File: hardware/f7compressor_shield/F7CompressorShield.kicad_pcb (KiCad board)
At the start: 2 copper layers, 148 x 168 mm, 12 parts, among them CN10 PinSocket_2x17_P2.54mm_Vertic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, CN7 PinSocket_2x10_P2.54mm_Vertic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, CN8 PinSocket_2x08_P2.54mm_Vertic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, CN9 PinSocket_2x15_P2.54mm_Vertic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, J1 PinSocket_2x17_P2.54mm_Vertic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, J2 PinHeader_1x06_P2.54mm_Vertic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, J3 TerminalBlock_MaiXu_MX126-5.0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, J4 TerminalBlock_MaiXu_MX126-5.0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, J5 TerminalBlock_MaiXu_MX126-5.0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, U1 ST_Morpho_Connector_144_STLink

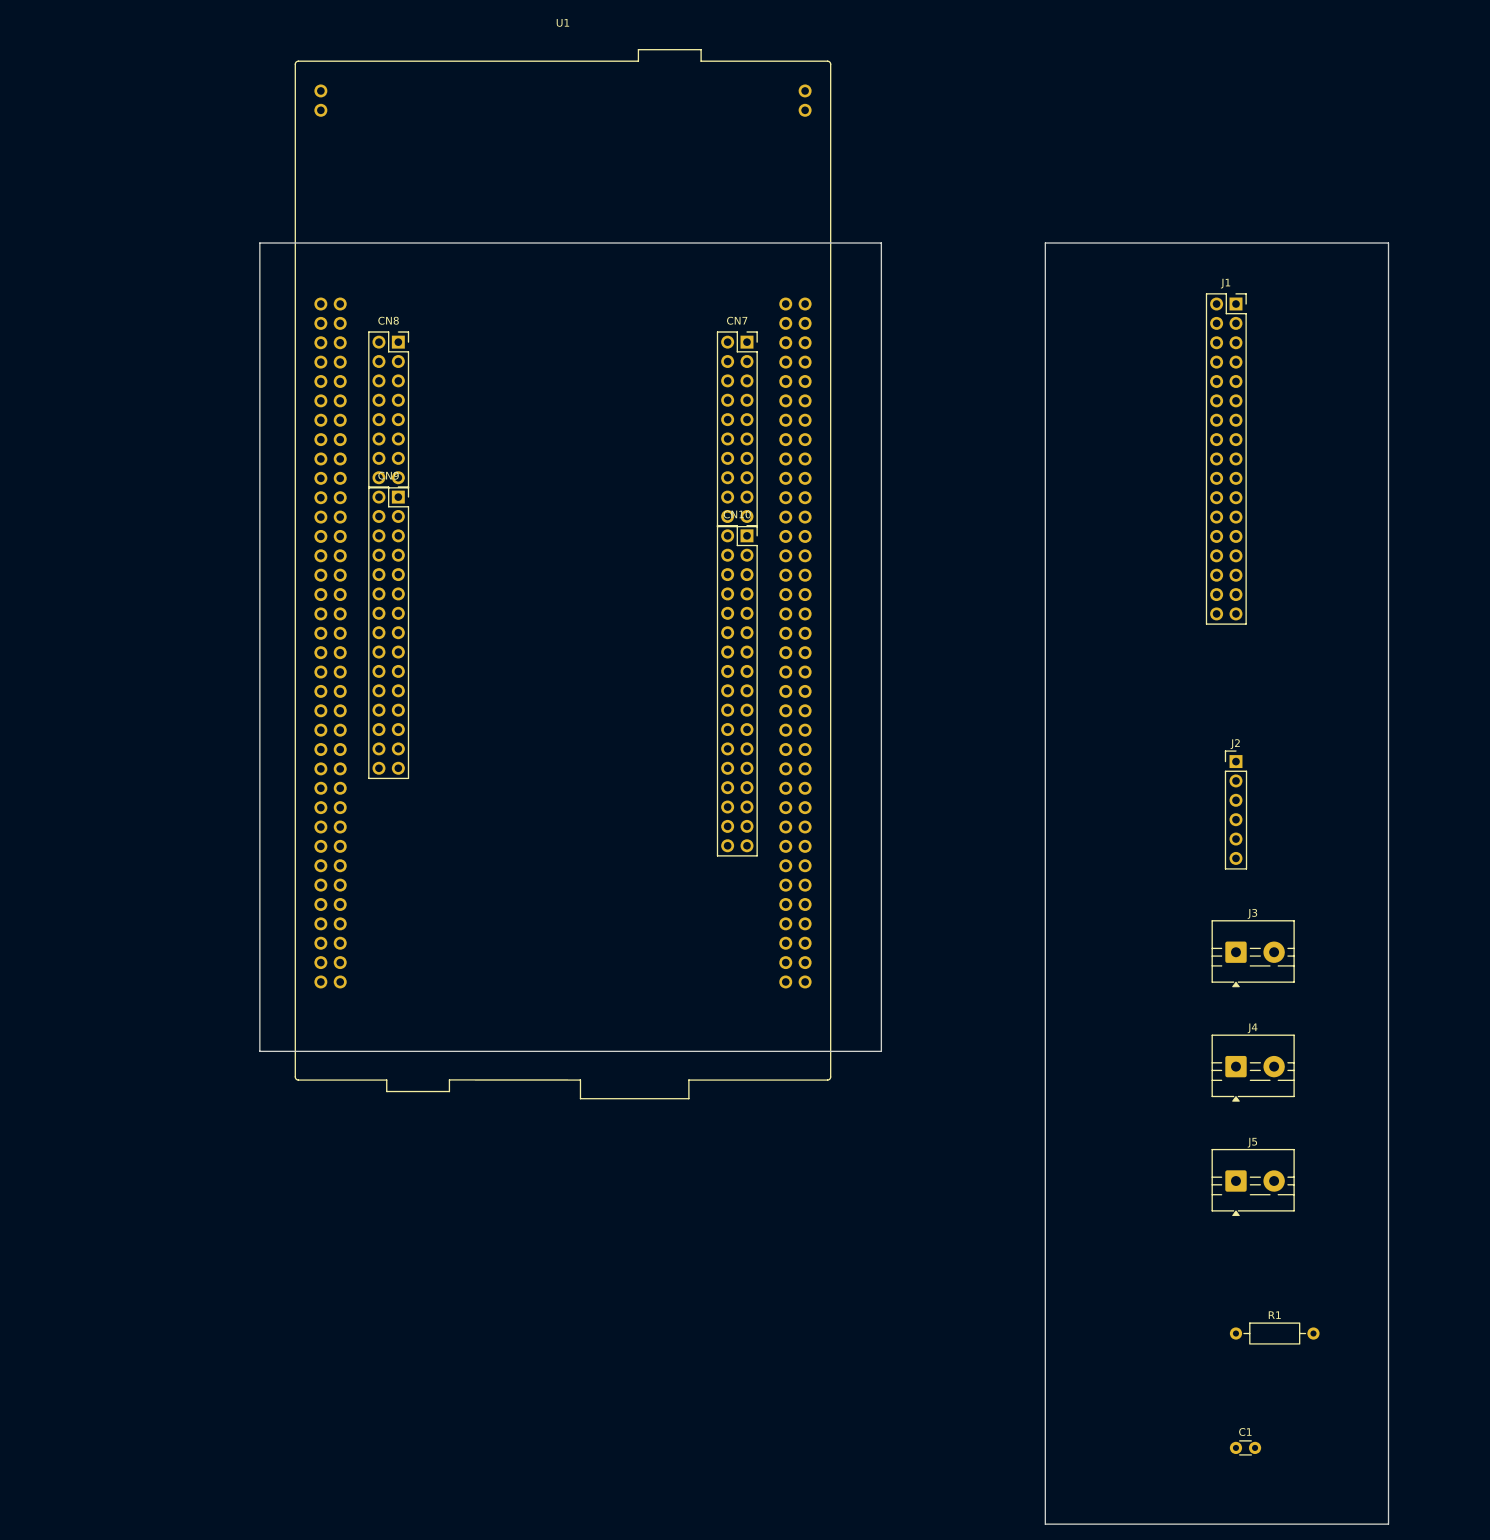
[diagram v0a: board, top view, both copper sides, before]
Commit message: Fix Zio/LCD header pin-1 orientation on shield PCB; re-route
Pin 1's physical column (and its square silkscreen marker) didn't match
the real Nucleo/LCD silkscreen on CN7-CN10 and J1 -- the generic KiCad
Odd_Even footprint's pad 1/2 assignment is mirrored relative to the real
boards. Fixed by mirroring the footprints themselves (not swapping net
assignments, which is electrically equivalent but leaves the pin-1
marker in the wrong physical spot). Also fixed 3 clearance violations
left by the re-route and confirmed CN12/FMC pin alternate-function
questions against the Nucleo schematic and MCU datasheet -- no other
conflicts beyond the already-documented PD8/PD9 VCP/FMC_D13-D14 reuse.

ERC clean, DRC 0 unconnected items, same expected-findings baseline.

Co-Authored-By: Claude Sonnet 5 <noreply@anthropic.com>
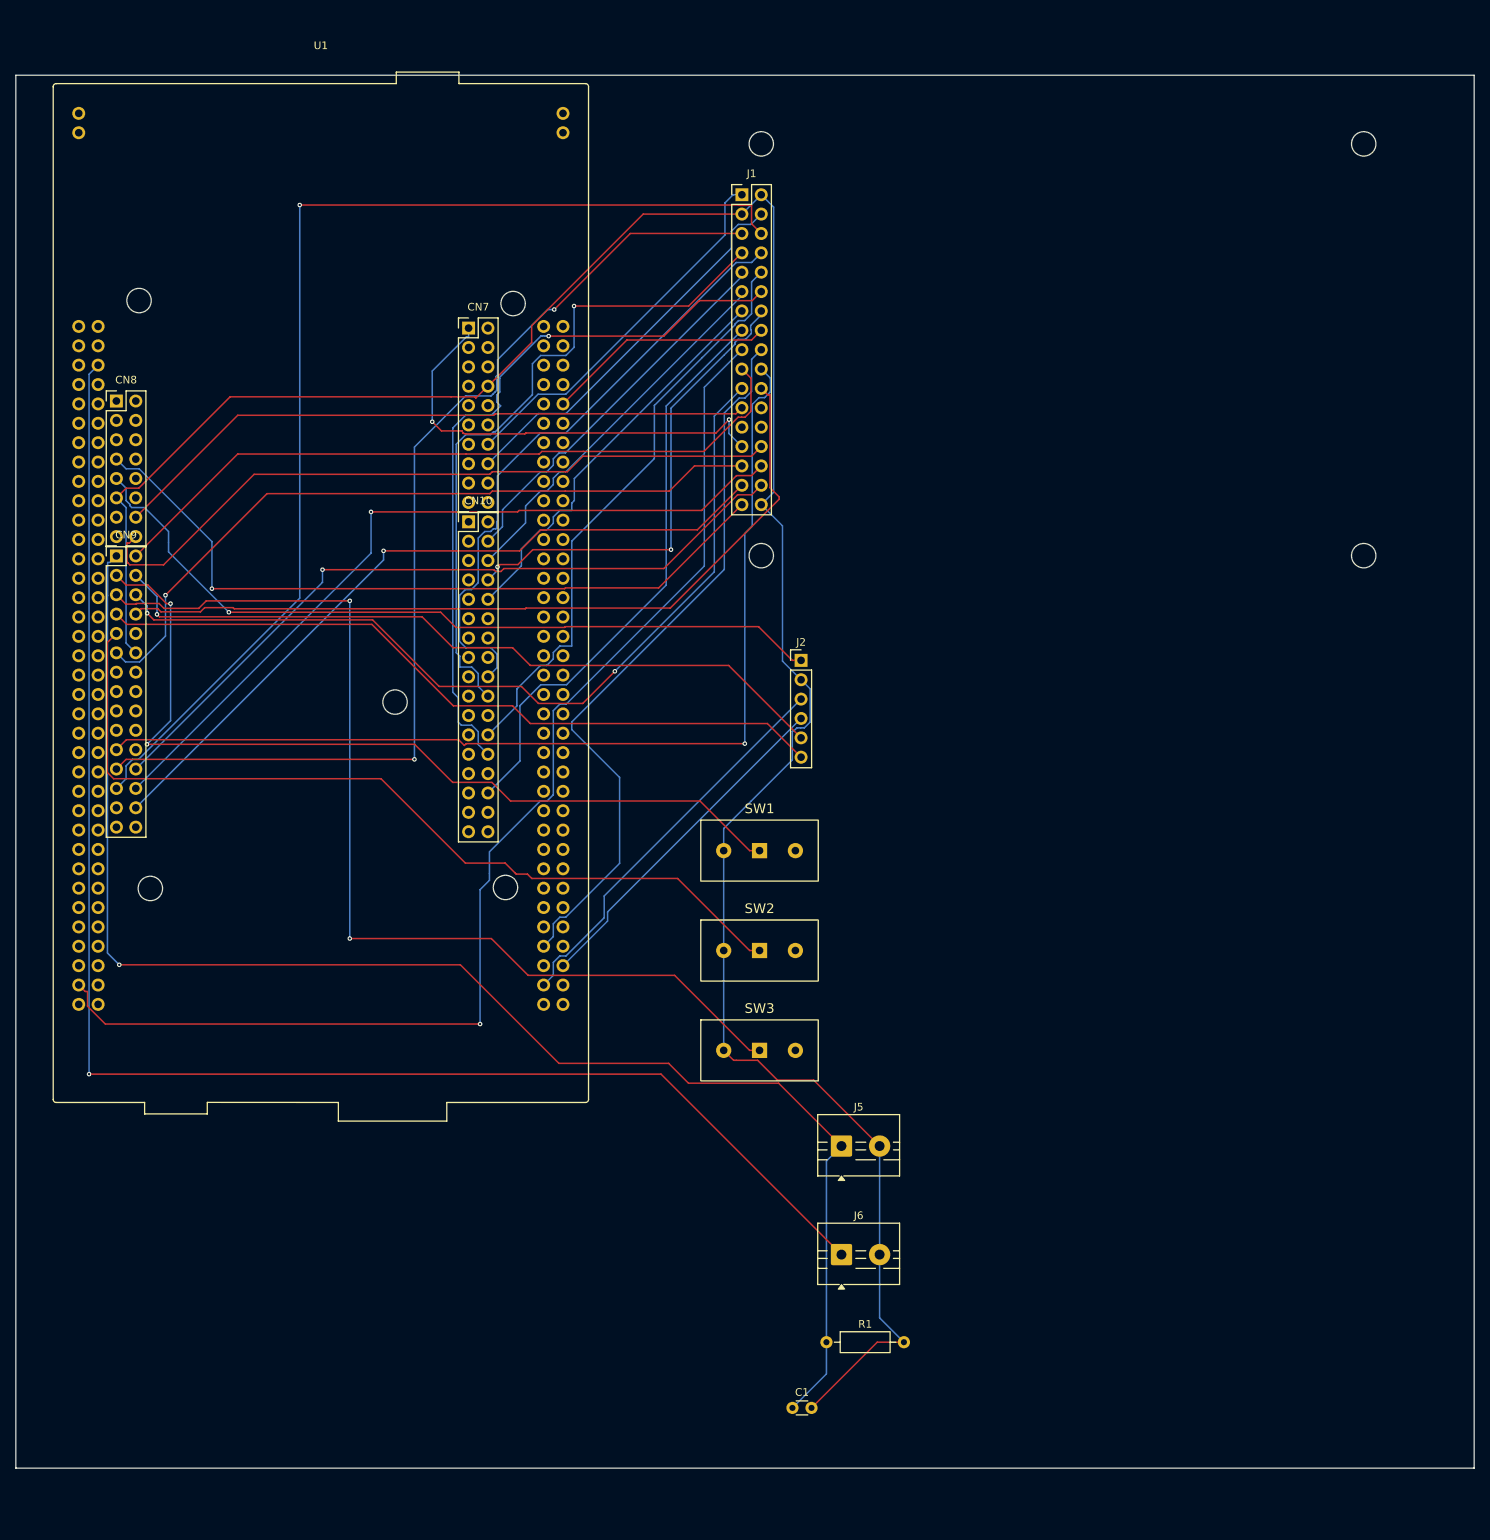
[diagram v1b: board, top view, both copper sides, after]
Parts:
- removed J3, J4: TerminalBlock_MaiXu_MX126-5.0-02P_1x02_P5.00mm, TerminalBlock_MaiXu_MX126-5.0-02P_1x02_P5.00mm
- added ?: MountingHole_3.2mm_M3, MountingHole_3.2mm_M3, F.Cu at (64.2, 106.5)
- added ?: MountingHole_3.2mm_M3, MountingHole_3.2mm_M3, F.Cu at (176.8, 9.00)
- added ?: MountingHole_3.2mm_M3, MountingHole_3.2mm_M3, F.Cu at (16.2, 29.5)
- added ?: MountingHole_3.2mm_M3, MountingHole_3.2mm_M3, F.Cu at (17.6, 106.6)
- added ?: MountingHole_3.2mm_M3, MountingHole_3.2mm_M3, F.Cu at (65.2, 29.9)
- added ?: MountingHole_3.2mm_M3, MountingHole_3.2mm_M3, F.Cu at (49.7, 82.2)
- added ?: MountingHole_3.2mm_M3, MountingHole_3.2mm_M3, F.Cu at (97.8, 63.0)
- added ?: MountingHole_3.2mm_M3, MountingHole_3.2mm_M3, F.Cu at (176.8, 63.0)
- added ?: MountingHole_3.2mm_M3, MountingHole_3.2mm_M3, F.Cu at (97.8, 9.00)
- added J6: TerminalBlock_MaiXu_MX126-5.0-02P_1x02_P5.00mm, TerminalBlock_MaiXu_MX126-5.0-02P_1x02_P5.00mm, F.Cu at (108.3, 154.7)
- added SW1: , , F.Cu at (92.8, 101.7)
- added SW2: , , F.Cu at (92.8, 114.8)
- added SW3: , , F.Cu at (92.8, 127.9)
- moved J1 63.9 mm to (97.8, 15.7)
- moved J2 58.6 mm to (103.0, 76.7)
- moved C1 58.4 mm to (101.8, 174.8)
- moved R1 53.7 mm to (106.3, 166.1)
- moved J5 51.9 mm to (108.3, 140.4)
- moved CN8 35.3 mm to (15.7, 42.7)
- moved CN9 35.3 mm to (15.7, 63.0)
- moved CN10 34.0 mm to (61.9, 58.6)
- moved CN7 34.0 mm to (61.9, 33.2)
- moved U1 31.9 mm to (8.25, 32.9)
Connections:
- CN9 pad 5: (no net) -> RUN_SENSE
- U1 pad 6: (no net) -> +5V_IN
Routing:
- net GND: track 0.00 -> 313.7 mm
- net +5V_IN: track 0.00 -> 201.9 mm, vias 0 -> 1
- net PRESSURE_SENSE: track 0.00 -> 196.5 mm, vias 0 -> 1
- net FMC_D14: track 0.00 -> 159.5 mm, vias 0 -> 1
- net FMC_D3: track 0.00 -> 150.4 mm, vias 0 -> 1
- net FMC_D2: track 0.00 -> 137.5 mm, vias 0 -> 2
- net RUN_SENSE: track 0.00 -> 135.9 mm, vias 0 -> 2
- net FMC_A0: track 0.00 -> 134.8 mm, vias 0 -> 1
- net FMC_NWE: track 0.00 -> 115.0 mm, vias 0 -> 2
- net OIL_SW: track 0.00 -> 114.5 mm, vias 0 -> 2
- net ESTOP: track 0.00 -> 113.9 mm
- net FMC_NOE: track 0.00 -> 106.8 mm
- net TP_SCK: track 0.00 -> 102.7 mm, vias 0 -> 1
- net +5V: track 0.00 -> 102.4 mm, vias 0 -> 1
- net TP_SDO: track 0.00 -> 98.6 mm, vias 0 -> 1
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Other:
- board size 148 x 168 mm -> 191.2 x 182.7 mm

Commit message: Split Morpho U1 into real CN11/CN12 connectors; fix place_mirrored() offset bug
CN11/CN12 were previously one combined ST footprint (148 pads, 8 more
than the real 140-pin total) representing two physically separate
connectors. Replaced with two separate 35x2 parts -- same footprint
family already pin-1-verified for CN7-CN10 -- using real pin numbers
from ST UM1974 Table 21, cross-checked against CLAUDE.md (all 6 signals
used here matched exactly).

While placing them, found that place_mirrored() was landing pad 1 one
full pin pitch (2.54mm) away from its intended position on every
connector it had touched (CN7-CN10, J1), not just the new ones -- the
hand-mirror step doesn't move the footprint's own anchor, so a naive
SetPosition(pos_mm) put pad 1 at pos_mm - 2.54mm instead of at pos_mm.
Fixed the function to solve for the anchor position that puts pad 1
exactly on target, and reverified all six mirrored connectors land
correctly.

Net effect: DRC findings dropped from 137 to 26 (splitting the combined
footprint removed most of its courtyard overlap with the Zio headers).
Re-routed and fixed the resulting clearance violations with verified
local detours (checked against pads and tracks, not just pads).

ERC clean, DRC 0 unconnected / 0 clearance violations.

Co-Authored-By: Claude Sonnet 5 <noreply@anthropic.com>
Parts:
- removed the ? at (64.2, 106.5)
- removed the ? at (16.2, 29.5)
- removed the ? at (17.6, 106.6)
- removed the ? at (65.2, 29.9)
- removed the ? at (49.7, 82.2)
- removed U1: ST_Morpho_Connector_144_STLink, ST_Morpho_Connector_144_STLink
- added ?: MountingHole_3.2mm_M3, MountingHole_3.2mm_M3, F.Cu at (65.2, 25.5)
- added ?: MountingHole_3.2mm_M3, MountingHole_3.2mm_M3, F.Cu at (64.2, 102.1)
- added ?: MountingHole_3.2mm_M3, MountingHole_3.2mm_M3, F.Cu at (49.7, 77.8)
- added ?: MountingHole_3.2mm_M3, MountingHole_3.2mm_M3, F.Cu at (17.6, 102.2)
- added ?: MountingHole_3.2mm_M3, MountingHole_3.2mm_M3, F.Cu at (16.2, 25.1)
- added CN11: PinSocket_2x35_P2.54mm_Vertical, PinSocket_2x35_P2.54mm_Vertical, F.Cu at (10.8, 28.5)
- added CN12: PinSocket_2x35_P2.54mm_Vertical, PinSocket_2x35_P2.54mm_Vertical, F.Cu at (71.8, 28.5)
- moved CN8 5.12 mm to (18.3, 38.3)
- moved CN9 5.12 mm to (18.3, 58.6)
- moved CN10 5.12 mm to (64.5, 54.1)
- moved CN7 5.12 mm to (64.5, 28.7)
- moved J1 2.54 mm to (100.3, 15.7)
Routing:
- net OIL_SW: track 114.5 -> 145.5 mm, vias 2 -> 1
- net FMC_NWE: track 115.0 -> 88.8 mm, vias 2 -> 0
- net FMC_D9: track 96.2 -> 73.6 mm, vias 1 -> 0
- net FMC_D4: track 89.1 -> 68.4 mm, vias 1 -> 0
- net FMC_D2: track 137.5 -> 156.2 mm
- net +3V3: track 97.2 -> 115.4 mm, vias 1 -> 2
- net ESTOP: track 113.9 -> 131.3 mm, vias 0 -> 1
- net LCD_RST: track 85.4 -> 101.1 mm, vias 0 -> 1
- net FMC_D13: track 30.0 -> 44.7 mm
- net FMC_NOE: track 106.8 -> 92.4 mm
- net RUN_SENSE: track 135.9 -> 150.1 mm, vias 2 -> 1
- net FMC_A0: track 134.8 -> 120.9 mm, vias 1 -> 0
- net TP_SCK: track 102.7 -> 115.9 mm, vias 1 -> 3
- net TP_IRQ: track 93.7 -> 104.9 mm
- net FMC_D14: track 159.5 -> 149.0 mm
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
